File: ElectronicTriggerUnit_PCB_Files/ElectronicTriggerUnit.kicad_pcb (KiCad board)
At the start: 2 copper layers, 44.4 x 29.3 mm, 36 parts, among them IC3 ATTINY816-MNR, J4 Conn_01x04, Q1 LC191PTDT, Q2 LKPT30102B-A01, Q3 78-SQRS140ELP, Q4 LC191PTDT, Q5 2N7002, Q8 SI7149ADP-T1-GE3, U2 12v, U3 GndMotor, U4 Gnd, U5 LM1117MP-5.0

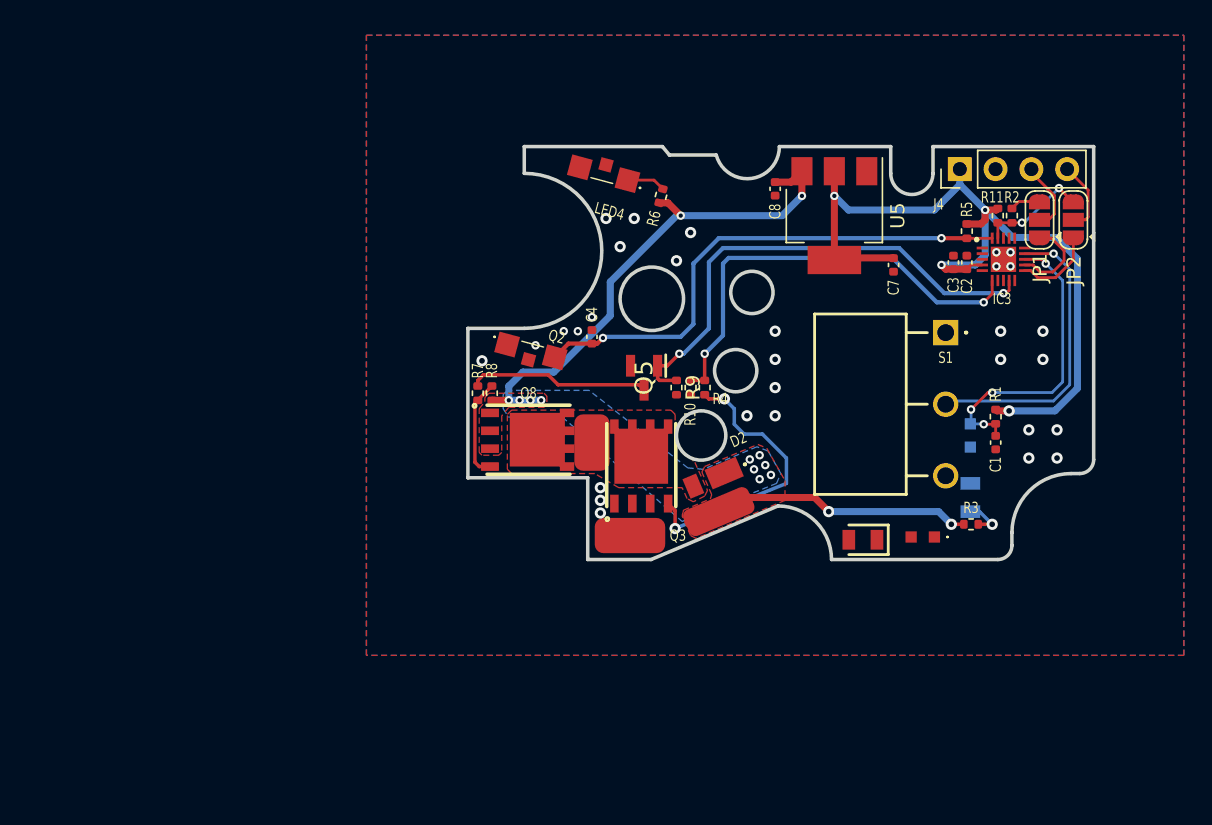
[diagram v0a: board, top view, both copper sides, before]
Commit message: modular board version
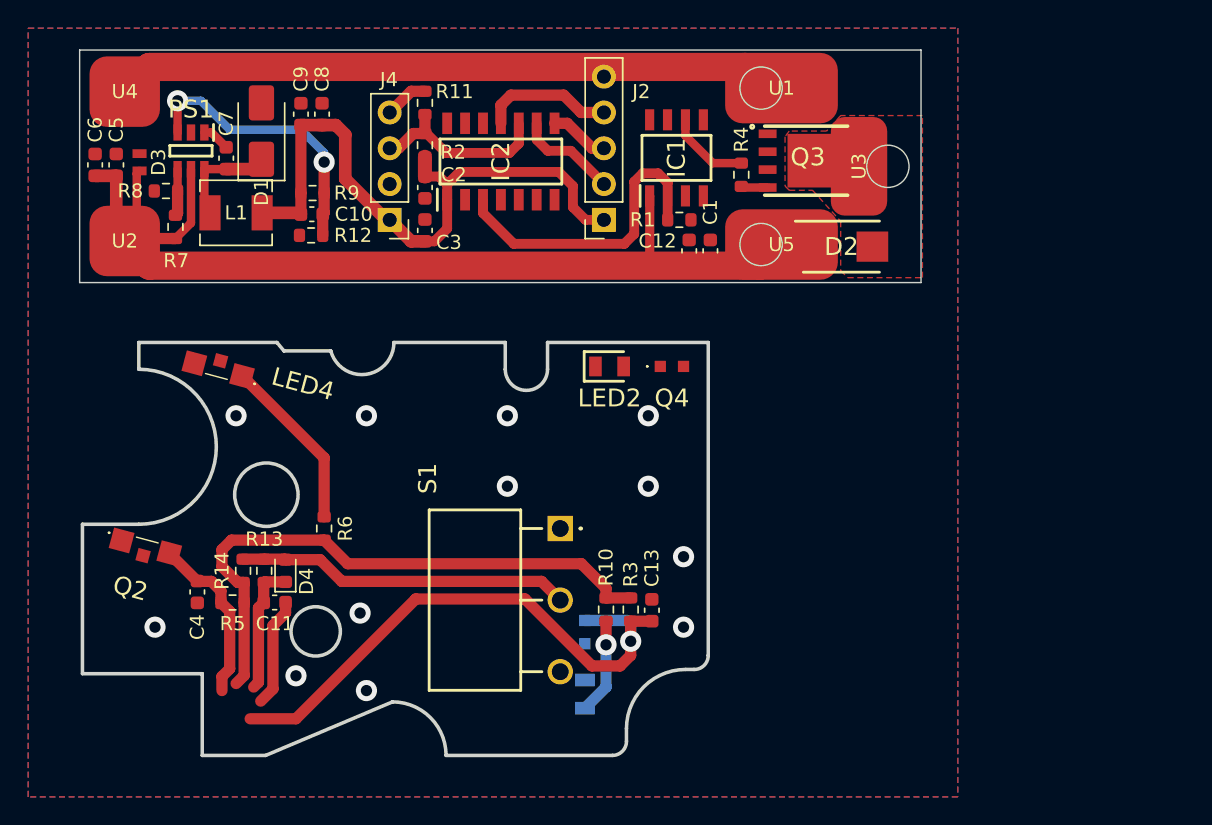
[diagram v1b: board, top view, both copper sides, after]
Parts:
- removed IC3: ATTINY816-MNR, SamacSys_Parts:QFN40P300X300X90-21N
- removed JP1, JP2: Jumper_3_Open, Jumper:SolderJumper-3_P1.3mm_Open_RoundedPad1.0x1.5mm
- removed Q5: 2N7002, SamacSys:SOT96P240X120-3N
- removed Q8: SI7149ADP-T1-GE3, SamacSys_Parts:POWERPAKSO-8
- added C10: 100p, Capacitor_SMD:C_0603_1608Metric, F.Cu at (81.1, 90.7)
- added C11: 100nf, Capacitor_SMD:C_0603_1608Metric, F.Cu at (78.5, 118.2)
- added C12: 0.1u, Capacitor_SMD:C_0603_1608Metric, F.Cu at (107.9, 93.3)
- added C13: 10n, Capacitor_SMD:C_0603_1608Metric, F.Cu at (105.2, 118.8)
- added C5: 10u/1206, Capacitor_SMD:C_0603_1608Metric, F.Cu at (67.2, 87.2)
- added C6: 10u/1206, Capacitor_SMD:C_0603_1608Metric, F.Cu at (65.8, 87.2)
- added C9: 22u, Capacitor_SMD:C_0603_1608Metric, F.Cu at (80.3, 83.6)
- added D1: B340A, Diode_SMD:D_SMA, F.Cu at (77.5, 84.8)
- added D3: 824045812, SamacSys:TVS_DIODE, F.Cu at (68.9, 87.0)
- added D4: D, Diode_SMD:D_0603_1608Metric, F.Cu at (79.2, 116.0)
- added IC1: MCP1407-E_SN, SamacSys:SOIC127P600X175-8N, F.Cu at (107.0, 86.7)
- added IC2: ATTINY814-SSF, SamacSys:SOIC127P600X175-14N, F.Cu at (94.5, 87.0)
- added J2: Conn_01x05, Connector_PinSocket_2.54mm:PinSocket_1x05_P2.54mm_Vertical, F.Cu at (101.8, 91.1)
- added L1: 10u/C2921170, Inductor_SMD:L_Chilisin_BMRA00040420, F.Cu at (75.8, 90.6)
- added PS1: AP5100WG-7, SamacSys:SOT95P285X140-6N, F.Cu at (72.5, 86.2)
- added R12: 3.3k, Resistor_SMD:R_0603_1608Metric, F.Cu at (81.1, 92.2)
- added R13: 1K, Resistor_SMD:R_0603_1608Metric, F.Cu at (77.8, 116.0)
- added R14: 10K, Resistor_SMD:R_0603_1608Metric, F.Cu at (76.2, 116.0)
- added U1: Gnd, SamacSys:Copper_Pad, F.Cu at (114.5, 81.8)
- C1, C2: value 10n -> 1u; footprint Capacitor_SMD:C_0402_1005Metric -> Capacitor_SMD:C_0603_1608Metric
- C3: value 1u -> 10n; footprint Capacitor_SMD:C_0402_1005Metric -> Capacitor_SMD:C_0603_1608Metric
- C4: footprint Capacitor_SMD:C_0402_1005Metric -> Capacitor_SMD:C_0603_1608Metric
- C7: value 1uF -> 22n; footprint Capacitor_SMD:C_0402_1005Metric -> Capacitor_SMD:C_0603_1608Metric
- C8: value 1uF -> 22u; footprint Capacitor_SMD:C_0402_1005Metric -> Capacitor_SMD:C_0603_1608Metric
- D2: value D -> SS24; footprint SamacSys_Parts:SBR3U60P1Q7 -> SamacSys:DIOM5436X247N
- LED1, LED2: footprint SamacSys_Parts:LEDC2012X105N -> SamacSys:LEDC2012X105N
- LED4, Q2: footprint SamacSys_Parts:APA3010P3C -> SamacSys:APA3010P3C
- Q1, Q4: footprint SamacSys_Parts:AP1608P1CP22 -> SamacSys:AP1608P1CP22
- Q3: footprint SamacSys_Parts:POWERPAKSO-8 -> SamacSys:POWERPAKSO-8
- R1, R5: footprint Resistor_SMD:R_0402_1005Metric -> Resistor_SMD:R_0603_1608Metric
- R10: value 10k -> 91R; footprint Resistor_SMD:R_0402_1005Metric -> Resistor_SMD:R_0603_1608Metric
- R11: value 10k -> 1k; footprint Resistor_SMD:R_0402_1005Metric -> Resistor_SMD:R_0603_1608Metric
- R2: value 1k -> 10k; footprint Resistor_SMD:R_0402_1005Metric -> Resistor_SMD:R_0603_1608Metric
- R3: value 680R -> 10k; footprint Resistor_SMD:R_0402_1005Metric -> Resistor_SMD:R_0603_1608Metric
- R4: value 4.7k -> 10R; footprint Resistor_SMD:R_0402_1005Metric -> Resistor_SMD:R_0603_1608Metric
- R6: value 680R -> 51R; footprint Resistor_SMD:R_0402_1005Metric -> Resistor_SMD:R_0603_1608Metric
- R7: value 4.7R -> 10k; footprint Resistor_SMD:R_0402_1005Metric -> Resistor_SMD:R_0603_1608Metric
- R8: value 2.2k -> 2k; footprint Resistor_SMD:R_0402_1005Metric -> Resistor_SMD:R_0603_1608Metric
- R9: value 2.2k -> 10k; footprint Resistor_SMD:R_0402_1005Metric -> Resistor_SMD:R_0603_1608Metric
- S1: footprint SamacSys_Parts:463092691402 -> SamacSys:463092691402
- U2, U3, U4: footprint SamacSys_Parts:Copper_pad -> SamacSys:Copper_Pad
- U5: value LM1117MP-5.0 -> 12v; footprint Package_TO_SOT_SMD:SOT-223-3_TabPin2 -> SamacSys:Copper_Pad
- moved R5 58.4 mm to (75.5, 118.2), turned to 0 degrees
- moved C7 48.0 mm to (75.0, 86.7), turned to -90 degrees
- moved U4 47.7 mm to (67.8, 82.0), turned to 0 degrees
- moved U2 46.3 mm to (67.8, 92.6), turned to 0 degrees
- moved R2 41.9 mm to (89.2, 85.8)
- moved R11 41.4 mm to (89.2, 82.8), turned to 90 degrees
- moved J4 40.6 mm to (86.7, 91.1), turned to 180 degrees
- moved C2 38.8 mm to (89.2, 88.8), turned to -90 degrees
- moved C3 37.6 mm to (89.2, 91.8)
- moved R6 33.6 mm to (82.0, 113.0), turned to 90 degrees
- moved C4 33.3 mm to (73.0, 117.5), turned to -90 degrees
- moved C8 32.6 mm to (81.8, 83.6)
- moved LED1 30.7 mm to (100.5, 124.8)
- moved Q1 30.7 mm to (100.5, 120.3)
- moved Q2 30.7 mm to (69.3, 114.3)
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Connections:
- C1 pad 1: /Semi_Auto -> GND
- C1 pad 2: GND -> +12V
- C2 pad 1: +5V -> +3.3V
- C3 pad 1: +5V -> +3.3V
- C4 pad 1: /V_Cycle -> /V_Cycle_Out
- C7 pad 1: GND -> Net-(PS1-BST)
- C7 pad 2: +5V -> Net-(D1-K)
- C8 pad 1: GND -> +3.3V
- C8 pad 2: +12V -> GND
- J4 pad 1: +5V -> +3.3V
- J4 pad 3: /updi/Tx -> /updiRx
- J4 pad 4: /updi/Rx -> /updiTx
- LED4 pad 1: GND -> Net-(LED4-Pad1)
- LED4 pad 2: Net-(LED4-Pad2) -> GND
- LED4 pad 3: (no net) -> GND
- Q2 pad 1: /V_Cycle -> GND
- Q2 pad 2: GND -> /V_Cycle_Out
- Q2 pad 3: (no net) -> GND
- R1 pad 1: /Semi_Auto -> GND
- R1 pad 2: +5V -> /NMOS
- R10 pad 1: GND -> +3.3V
- R10 pad 2: /NMOS -> Net-(LED1-Pad2)
- R11 pad 1: +5V -> /updiRx
- R11 pad 2: /updiRx -> /updiTx
- R2 pad 1: /updiRx -> +3.3V
- R2 pad 2: /updiTx -> /updiRx
- R3 pad 1: +12V -> /Semi_Auto
- R3 pad 2: Net-(LED1-Pad2) -> +3.3V
- R4 pad 1: /NMOS -> Net-(Q3-Pad4)
- R4 pad 2: Net-(Q3-Pad4) -> Net-(IC1-OUT_1)
- R5 pad 1: /V_Cycle -> /V_Cycle_Out
- R5 pad 2: +5V -> +3.3V
- R6 pad 1: +12V -> +3.3V
- R6 pad 2: Net-(LED4-Pad2) -> Net-(LED4-Pad1)
- R7 pad 1: Net-(Q5-D) -> Net-(PS1-EN)
- R7 pad 2: Net-(Q8-G) -> +12V
- R8 pad 1: +12V -> GND
- R8 pad 2: Net-(Q8-G) -> Net-(PS1-EN)
- R9 pad 1: /ACTIVE_BREAK -> +3.3V
- R9 pad 2: GND -> /V_FB
- S1 pad 2: /trigger -> Net-(D4-A)
- U5 pad 1: GND -> +12V
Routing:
- net +3.3V: track 0.00 -> 87.2 mm
- net +5V: track 60.8 -> 0.00 mm, vias 4 -> 0
- net GND: track 0.00 -> 56.3 mm, vias 30 -> 12
- net /V_Cycle: track 37.1 -> 0.00 mm, vias 2 -> 0
- net /ACTIVE_BREAK: track 35.6 -> 0.00 mm, vias 2 -> 0
- net Net-(D4-A): track 0.00 -> 23.7 mm
- net /trigger: track 21.6 -> 0.00 mm, vias 1 -> 0
- net /V_FB: track 0.00 -> 20.1 mm, vias 0 -> 2
- net /Semi_Auto: track 21.6 -> 41.3 mm, vias 4 -> 1
- net Net-(Q3-Pad4): track 20.6 -> 1.90 mm, vias 2 -> 0
- net +12V: track 56.8 -> 73.7 mm, vias 14 -> 0
- net Net-(Q5-D): track 12.8 -> 0.00 mm
- net Net-(LED4-Pad1): track 0.00 -> 12.4 mm
- net /V_Cycle_Out: track 0.00 -> 12.3 mm
- net /NMOS: track 31.6 -> 22.1 mm, vias 2 -> 0
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- removed copper zone on B.Cu, net +12V
- removed copper zone on F.Cu, net +12V
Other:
- board size 44.4 x 29.3 mm -> 59.7 x 50 mm
